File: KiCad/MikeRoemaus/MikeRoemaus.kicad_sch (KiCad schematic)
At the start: 14 parts, among them J1 Conn_01x04_Socket, J2 Conn_01x04_Socket, J3 Conn_01x02_Socket, SW1 SW_DIP_x01, SW2 SW_DIP_x03

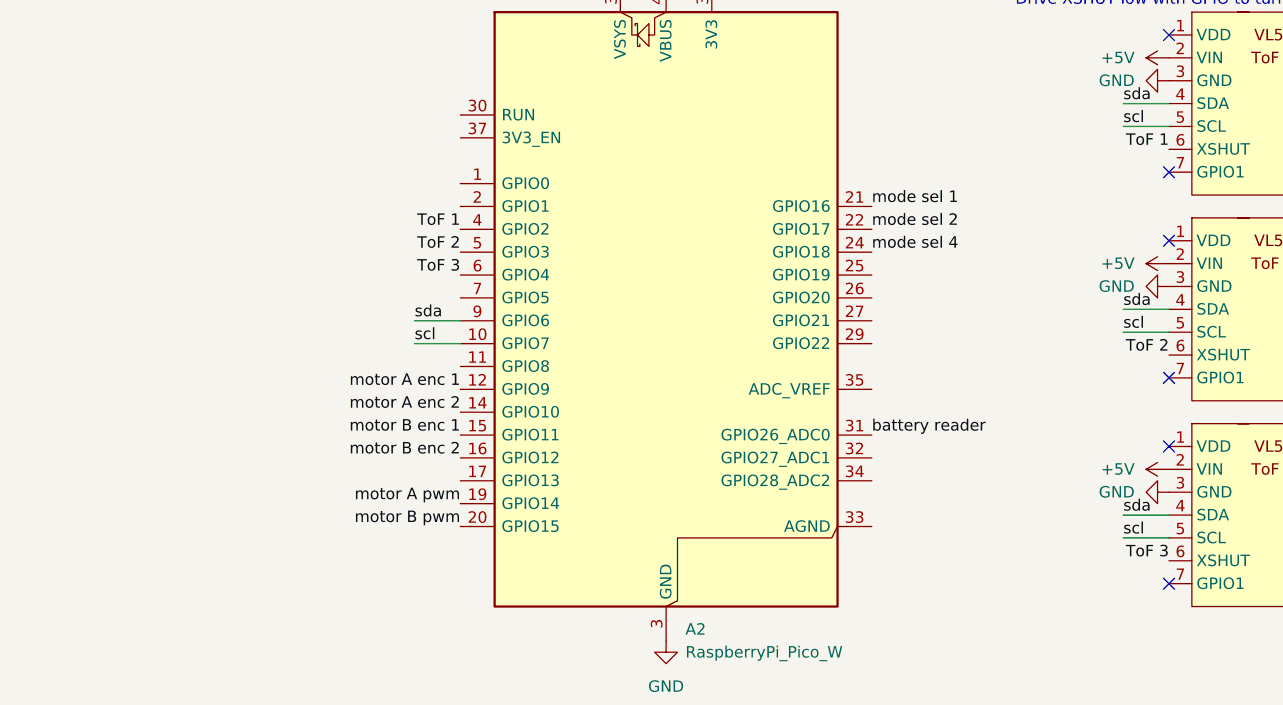
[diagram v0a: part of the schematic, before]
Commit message: resized pcb and added breakout gpio. still need to reroute and add capacitors
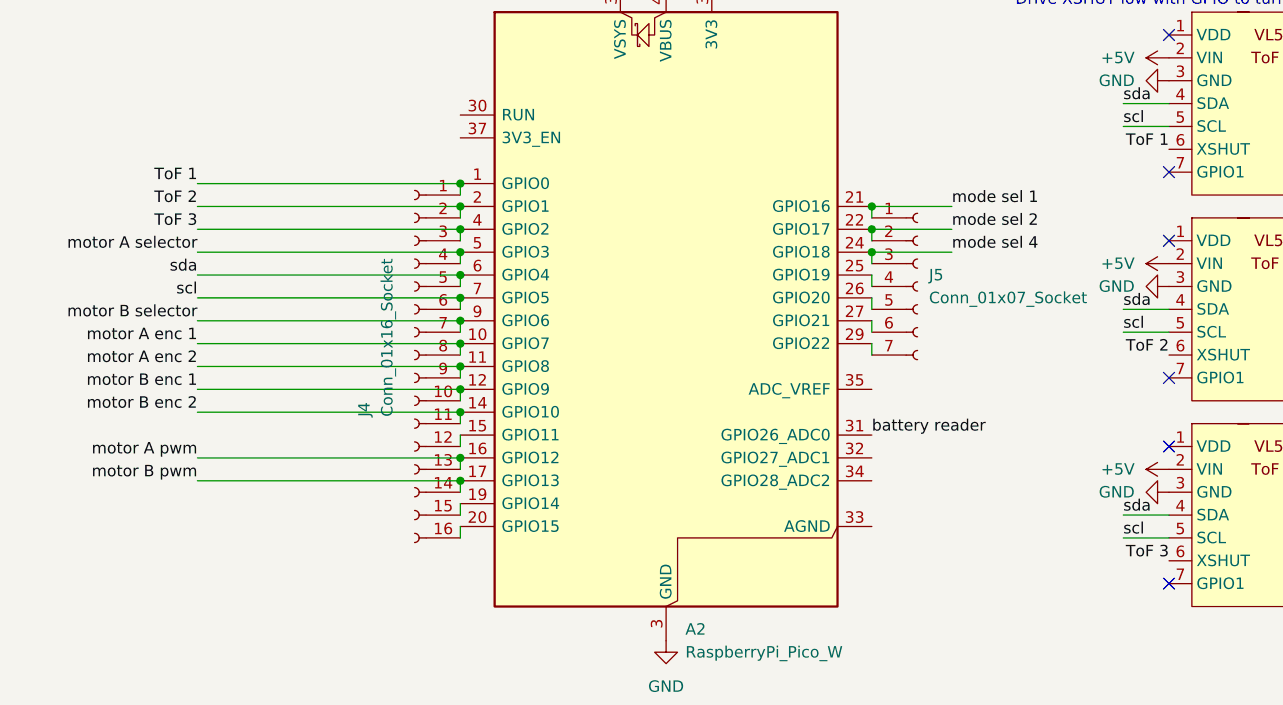
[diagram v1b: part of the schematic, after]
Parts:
- added J4: Conn_01x16_Socket, Connector_PinSocket_2.54mm:PinSocket_1x16_P2.54mm_Vertical, symbol Connector:Conn_01x16_Socket
- added J5: Conn_01x07_Socket, Connector_PinSocket_2.54mm:PinSocket_1x07_P2.54mm_Vertical, symbol Connector:Conn_01x07_Socket
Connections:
- net ToF 1: now also A2.1 (GPIO0), J4.1 (Pin_1); no longer A2.4 (GPIO2)
- net ToF 2: now also A2.2 (GPIO1), J4.2 (Pin_2); no longer A2.5 (GPIO3)
- net ToF 3: now also A2.4 (GPIO2), J4.3 (Pin_3); no longer A2.6 (GPIO4)
- net mode sel 1: now also J5.1 (Pin_1)
- net mode sel 2: now also J5.2 (Pin_2)
- net mode sel 4: now also J5.3 (Pin_3)
- net motor A enc 1: now also A2.10 (GPIO7), J4.8 (Pin_8); no longer A2.12 (GPIO9)
- net motor A enc 2: now also A2.11 (GPIO8), J4.9 (Pin_9); no longer A2.14 (GPIO10)
- net motor A pwm: now also A2.16 (GPIO12), J4.13 (Pin_13); no longer A2.19 (GPIO14)
- net motor A selector: now also A2.5 (GPIO3), J4.4 (Pin_4)
- net motor B enc 1: now also A2.12 (GPIO9), J4.10 (Pin_10); no longer A2.15 (GPIO11)
- net motor B enc 2: now also A2.14 (GPIO10), J4.11 (Pin_11); no longer A2.16 (GPIO12)
- net motor B pwm: now also A2.17 (GPIO13), J4.14 (Pin_14); no longer A2.20 (GPIO15)
- net motor B selector: now also A2.9 (GPIO6), J4.7 (Pin_7)
- net scl: now also A2.7 (GPIO5), J4.6 (Pin_6); no longer A2.10 (GPIO7)
- net sda: now also A2.6 (GPIO4), J4.5 (Pin_5); no longer A2.9 (GPIO6)
- net at A2.25 (GPIO19): now also J5.4 (Pin_4)
- net at A2.26 (GPIO20): now also J5.5 (Pin_5)
- net at A2.27 (GPIO21): now also J5.6 (Pin_6)
- net at A2.29 (GPIO22): now also J5.7 (Pin_7)
- new net: A2.15 (GPIO11), J4.12 (Pin_12)
- new net: A2.19 (GPIO14), J4.15 (Pin_15)
- new net: A2.20 (GPIO15), J4.16 (Pin_16)

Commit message: done with pcb (PLEASE) “Free at last, Free at last, Thank God almighty we are free at last. — Martin Luther King Jr.
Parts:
- removed SW1: SW_DIP_x01, Button_Switch_SMD:SW_DIP_SPSTx01_Slide_9.78x4.72mm_W8.61mm_P2.54mm, symbol Switch:SW_DIP_x01
- added C1, C2: C, Resistor_THT:R_Axial_DIN0207_L6.3mm_D2.5mm_P7.62mm_Horizontal, symbol Device:C
- added C3: 470uF, Capacitor_THT:CP_Axial_L11.0mm_D8.0mm_P15.00mm_Horizontal, symbol Device:C
- added C4: 1uF, Capacitor_THT:CP_Axial_L11.0mm_D8.0mm_P15.00mm_Horizontal, symbol Device:C
- added C5: 0.1uF, Capacitor_THT:CP_Axial_L11.0mm_D8.0mm_P15.00mm_Horizontal, symbol Device:C
- added J6, J7: Conn_01x02_Socket, Connector_PinSocket_2.54mm:PinSocket_1x02_P2.54mm_Vertical, symbol Connector:Conn_01x02_Socket
- added R3: 10K, Resistor_THT:R_Axial_DIN0207_L6.3mm_D2.5mm_P7.62mm_Horizontal, symbol Device:R
- added SW1: SW_SPDT, mike_lib:pwr sw, symbol Switch:SW_SPDT
- added SW3: SW_DIP_x01, Button_Switch_THT:SW_DIP_SPSTx01_Slide_9.78x4.72mm_W7.62mm_P2.54mm, symbol Switch:SW_DIP_x01
- SW2: footprint Button_Switch_SMD:SW_DIP_SPSTx03_Slide_9.78x9.8mm_W8.61mm_P2.54mm -> Button_Switch_THT:SW_DIP_SPSTx03_Slide_9.78x9.8mm_W7.62mm_P2.54mm
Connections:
- net +3.3V: now also J7.1 (Pin_1)
- net +5V: now also J7.2 (Pin_2), SW3.1; no longer U6.7 (MODE)
- net GND: now also J6.1 (Pin_1), J6.2 (Pin_2), R3.1; no longer U6.14 (GND)
- net ToF 1: now also A2.5 (GPIO3), J4.4 (Pin_4); no longer A2.1 (GPIO0), J4.1 (Pin_1)
- net ToF 2: now also A2.6 (GPIO4), J4.5 (Pin_5); no longer A2.2 (GPIO1), J4.2 (Pin_2)
- net ToF 3: now also A2.7 (GPIO5), J4.6 (Pin_6); no longer A2.4 (GPIO2), J4.3 (Pin_3)
- net motor A +out: now also C1.1
- net motor A -out: now also C1.2
- net motor A selector: now also A2.4 (GPIO2), J4.3 (Pin_3); no longer A2.5 (GPIO3), J4.4 (Pin_4)
- net motor B +out: now also C2.1
- net motor B -out: now also C2.2
- net scl: now also A2.20 (GPIO15), J4.16 (Pin_16); no longer A2.7 (GPIO5), J4.6 (Pin_6)
- net sda: now also A2.19 (GPIO14), J4.15 (Pin_15); no longer A2.6 (GPIO4), J4.5 (Pin_5)
- net BAT + for motors: now reaches R1.1, U5.3 (VIN)
- net BAT + for motors: now also U6.13 (VIN), C3.2, C4.2, C5.2, SW1.3 (C)
- net +7.5V: no longer names the net of J3.1 (Pin_1)
- net +7.5V: now also SW1.2 (B); no longer U6.13 (VIN)
- new net: A2.1 (GPIO0), J4.1 (Pin_1)
- new net: A2.2 (GPIO1), J4.2 (Pin_2)
- new net: C3.1, C4.1, C5.1, U6.14 (GND)
- new net: R3.2, SW3.2, U6.7 (MODE)
- no-connect marks 12 -> 13
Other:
- note removed: "we want mode 1"
- moved on the sheet: J1, J2, J3, R1, R2, SW2, U1, U5, U6

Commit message: done, but actually this time remember to thicken BAT PWR traces, and add screws
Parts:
- added H2, H3, H4: MountingHole, MountingHole:MountingHole_3.5mm, symbol Mechanical:MountingHole
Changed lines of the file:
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@@
+	)
+	(symbol
+		(lib_id "Mechanical:MountingHole")
+		(at 170.18 138.43 0)
+		(unit 1)
+		(body_style 1)
+		(exclude_from_sim no)
+		(in_bom no)
+		(on_board yes)
+		(in_pos_files yes)
+		(dnp no)
+		(fields_autoplaced yes)
+		(property "Reference" "H2"
+			(at 172.72 137.1599 0)
+			(show_name no)
+			(do_not_autoplace no)
+			(effects
+				(font
+					(size 1.27 1.27)
+				)
+				(justify left)
+			)
+		)
+		(property "Value" "MountingHole"
+			(at 172.72 139.6999 0)
+			(show_name no)
+			(do_not_autoplace no)
+			(effects
+				(font
+					(size 1.27 1.27)
+				)
+				(justify left)
+			)
+		)
+		(property "Footprint" "MountingHole:MountingHole_3.5mm"
+			(at 170.18 138.43 0)
+			(hide yes)
+			(show_name no)
+			(do_not_autoplace no)
+			(effects
+				(font
+					(size 1.27 1.27)
+				)
+			)
+		)
+		(property "Datasheet" ""
+			(at 170.18 138.43 0)
+			(hide yes)
+			(show_name no)
+			(do_not_autoplace no)
+			(effects
+				(font
+					(size 1.27 1.27)
+				)
+			)
+		)
+		(property "Description" "Mounting Hole without connection"
+			(at 170.18 138.43 0)
+			(hide yes)
+			(show_name no)
+			(do_not_autoplace no)
+			(effects
+				(font
+					(size 1.27 1.27)
+				)
+			)
+		)
+		(instances
+			(project "MikeRoemaus"
+				(path "/1054ffa4-0d3c-4222-9dda-35d29dac0af1"
+					(reference "H2")
+					(unit 1)
+				)
+			)
+		)
 	)
 	(symbol
@@
 	)
 	(symbol
+		(lib_id "Mechanical:MountingHole")
+		(at 170.18 148.59 0)
+		(unit 1)
+		(body_style 1)
+		(exclude_from_sim no)
+		(in_bom no)
+		(on_board yes)
+		(in_pos_files yes)
+		(dnp no)
+		(fields_autoplaced yes)
+		(property "Reference" "H4"
+			(at 172.72 147.3199 0)
+			(show_name no)
+			(do_not_autoplace no)
+			(effects
+				(font
+					(size 1.27 1.27)
+				)
+				(justify left)
+			)
+		)
+		(property "Value" "MountingHole"
+			(at 172.72 149.8599 0)
+			(show_name no)
+			(do_not_autoplace no)
+			(effects
+				(font
+					(size 1.27 1.27)
+				)
+				(justify left)
+			)
+		)
+		(property "Footprint" "MountingHole:MountingHole_3.5mm"
+			(at 170.18 148.59 0)
+			(hide yes)
+			(show_name no)
+			(do_not_autoplace no)
+			(effects
+				(font
+					(size 1.27 1.27)
+				)
+			)
+		)
+		(property "Datasheet" ""
+			(at 170.18 148.59 0)
+			(hide yes)
+			(show_name no)
+			(do_not_autoplace no)
+			(effects
+				(font
+					(size 1.27 1.27)
+				)
+			)
+		)
+		(property "Description" "Mounting Hole without connection"
+			(at 170.18 148.59 0)
+			(hide yes)
+			(show_name no)
+			(do_not_autoplace no)
+			(effects
+				(font
+					(size 1.27 1.27)
+				)
+			)
+		)
+		(instances
+			(project "MikeRoemaus"
+				(path "/1054ffa4-0d3c-4222-9dda-35d29dac0af1"
+					(reference "H4")
+					(unit 1)
+				)
+			)
+		)
+	)
+	(symbol
 		(lib_id "Device:R")
 		(at 193.04 102.87 180)
@@
 					(unit 1)
 				)
+			)
+		)
+	)
+	(symbol
+		(lib_id "Mechanical:MountingHole")
+		(at 170.18 143.51 0)
+		(unit 1)
+		(body_style 1)
+		(exclude_from_sim no)
+		(in_bom no)
+		(on_board yes)
+		(in_pos_files yes)
+		(dnp no)
+		(fields_autoplaced yes)
+		(property "Reference" "H3"
+			(at 172.72 142.2399 0)
+			(show_name no)
+			(do_not_autoplace no)
+			(effects
+				(font
+					(size 1.27 1.27)
+				)
+				(justify left)
+			)
+		)
+		(property "Value" "MountingHole"
+			(at 172.72 144.7799 0)
+			(show_name no)
+			(do_not_autoplace no)
+			(effects
+				(font
+					(size 1.27 1.27)
+				)
+				(justify left)
+			)
+		)
+		(property "Footprint" "MountingHole:MountingHole_3.5mm"
+			(at 170.18 143.51 0)
+			(hide yes)
+			(show_name no)
+			(do_not_autoplace no)
+			(effects
+				(font
+					(size 1.27 1.27)
+				)
+			)
+		)
+		(property "Datasheet" ""
+			(at 170.18 143.51 0)
+			(hide yes)
+			(show_name no)
+			(do_not_autoplace no)
+			(effects
+				(font
+					(size 1.27 1.27)
+				)
+			)
+		)
+		(property "Description" "Mounting Hole without connection"
+			(at 170.18 143.51 0)
+			(hide yes)
+			(show_name no)
+			(do_not_autoplace no)
+			(effects
+				(font
+					(size 1.27 1.27)
+				)
+			)
+		)
+		(instances
+			(project "MikeRoemaus"
+				(path "/1054ffa4-0d3c-4222-9dda-35d29dac0af1"
+					(reference "H3")
+					(unit 1)
+				)

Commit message: motor centered now
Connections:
- net GND: now also C3.1, C4.1, C5.1, U6.14 (GND)
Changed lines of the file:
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@@
 	)
 	(junction
+		(at 114.3 113.03)
+		(diameter 0)
+		(color 0 0 0 0)
+	)
+	(junction
 		(at 66.04 77.47)
 		(diameter 0)
@@
 	(wire
 		(pts
+			(xy 114.3 113.03) (xy 127 113.03)
+		)
+		(stroke
+			(width 0)
+			(type default)
+		)
+	)
+	(wire
+		(pts
 			(xy 201.93 36.83) (xy 201.93 41.91)
 		)
@@
 					(unit 1)
 				)
+			)
+		)
+	)
+	(symbol
+		(lib_id "power:GND")
+		(at 127 113.03 90)
+		(unit 1)
+		(body_style 1)
+		(exclude_from_sim no)
+		(in_bom yes)
+		(on_board yes)
+		(in_pos_files yes)
+		(dnp no)
+		(fields_autoplaced yes)
+		(property "Reference" "#PWR027"
+			(at 133.35 113.03 0)
+			(hide yes)
+			(show_name no)
+			(do_not_autoplace no)
+			(effects
+				(font
+					(size 1.27 1.27)
+				)
+			)
+		)
+		(property "Value" "GND"
+			(at 130.81 113.0299 90)
+			(show_name no)
+			(do_not_autoplace no)
+			(effects
+				(font
+					(size 1.27 1.27)
+				)
+				(justify right)
+			)
+		)
+		(property "Footprint" ""
+			(at 127 113.03 0)
+			(hide yes)
+			(show_name no)
+			(do_not_autoplace no)
+			(effects
+				(font
+					(size 1.27 1.27)
+				)
+			)
+		)
+		(property "Datasheet" ""
+			(at 127 113.03 0)
+			(hide yes)
+			(show_name no)
+			(do_not_autoplace no)
+			(effects
+				(font
+					(size 1.27 1.27)
+				)
+			)
+		)
+		(property "Description" "Power symbol creates a global label with name \"GND\" , ground"
+			(at 127 113.03 0)
+			(hide yes)
+			(show_name no)
+			(do_not_autoplace no)
+			(effects
+				(font
+					(size 1.27 1.27)
+				)
+			)
+		)
+		(pin "1"
+		)
+		(instances
+			(project "MikeRoemaus"
+				(path "/1054ffa4-0d3c-4222-9dda-35d29dac0af1"
+					(reference "#PWR027")
+					(unit 1)
+				)
